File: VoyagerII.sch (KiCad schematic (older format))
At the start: 29 parts, among them P1 TC2030-IDC, SW1 SW_PUSH, U1 ATXMEGA32A4U-AU, U2 MCP1700T-3002E/TT, U3 PRTR5V0U2X, U4 IS31FL3731-SALS2

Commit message: Temporary progress save
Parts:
- R8, R9: renamed from R?; footprint (none) -> Resistors_SMD:R_0805
- gave numbers to parts that had none: 5
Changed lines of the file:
@@
 $EndComp
 $Comp
-L GND #PWR06
+L GND #PWR05
 U 1 1 5A624D2D
 P 4300 1500
-F 0 "#PWR06" H 4300 1250 50  0001 C CNN
+F 0 "#PWR05" H 4300 1250 50  0001 C CNN
 F 1 "GND" H 4300 1350 50  0000 C CNN
 F 2 "" H 4300 1500 50  0001 C CNN
@@
 $EndComp
 $Comp
-L +3.3V #PWR07
+L +3.3V #PWR06
 U 1 1 5A625634
 P 2550 2300
-F 0 "#PWR07" H 2550 2150 50  0001 C CNN
+F 0 "#PWR06" H 2550 2150 50  0001 C CNN
 F 1 "+3.3V" H 2550 2440 50  0000 C CNN
 F 2 "" H 2550 2300 50  0000 C CNN
@@
 $EndComp
 $Comp
-L GND #PWR08
+L GND #PWR07
 U 1 1 5A625723
 P 1900 2500
-F 0 "#PWR08" H 1900 2250 50  0001 C CNN
+F 0 "#PWR07" H 1900 2250 50  0001 C CNN
 F 1 "GND" H 1900 2350 50  0000 C CNN
 F 2 "" H 1900 2500 50  0000 C CNN
@@
 PDI_CLK
 $Comp
-L GND #PWR09
+L GND #PWR08
 U 1 1 5A62606A
 P 1650 2625
-F 0 "#PWR09" H 1650 2375 50  0001 C CNN
+F 0 "#PWR08" H 1650 2375 50  0001 C CNN
 F 1 "GND" H 1650 2475 50  0000 C CNN
 F 2 "" H 1650 2625 50  0000 C CNN
@@
 PDI
 $Comp
-L +3.3V #PWR010
+L +3.3V #PWR09
 U 1 1 5A6265F5
 P 3575 2050
-F 0 "#PWR010" H 3575 1900 50  0001 C CNN
+F 0 "#PWR09" H 3575 1900 50  0001 C CNN
 F 1 "+3.3V" H 3575 2190 50  0000 C CNN
 F 2 "" H 3575 2050 50  0000 C CNN
@@
 $EndComp
 $Comp
-L GND #PWR011
+L GND #PWR010
 U 1 1 5A626934
 P 3825 4950
-F 0 "#PWR011" H 3825 4700 50  0001 C CNN
+F 0 "#PWR010" H 3825 4700 50  0001 C CNN
 F 1 "GND" H 3825 4800 50  0000 C CNN
 F 2 "" H 3825 4950 50  0000 C CNN
@@
 $EndComp
 $Comp
-L +3.3V #PWR012
+L +3.3V #PWR011
 U 1 1 5A627061
 P 725 3075
-F 0 "#PWR012" H 725 2925 50  0001 C CNN
+F 0 "#PWR011" H 725 2925 50  0001 C CNN
 F 1 "+3.3V" H 725 3215 50  0000 C CNN
 F 2 "" H 725 3075 50  0000 C CNN
@@
 $EndComp
 $Comp
-L GND #PWR013
+L GND #PWR012
 U 1 1 5A62709B
 P 725 3275
-F 0 "#PWR013" H 725 3025 50  0001 C CNN
+F 0 "#PWR012" H 725 3025 50  0001 C CNN
 F 1 "GND" H 725 3125 50  0000 C CNN
 F 2 "" H 725 3275 50  0000 C CNN
@@
 $EndComp
 $Comp
-L +3.3V #PWR014
+L +3.3V #PWR013
 U 1 1 5A62AFDE
 P 1650 2425
-F 0 "#PWR014" H 1650 2275 50  0001 C CNN
+F 0 "#PWR013" H 1650 2275 50  0001 C CNN
 F 1 "+3.3V" H 1650 2565 50  0000 C CNN
 F 2 "" H 1650 2425 50  0001 C CNN
@@
 $EndComp
 $Comp
-L GND #PWR015
+L GND #PWR014
 U 1 1 5A64D83E
 P 5600 3550
-F 0 "#PWR015" H 5600 3300 50  0001 C CNN
+F 0 "#PWR014" H 5600 3300 50  0001 C CNN
 F 1 "GND" H 5600 3400 50  0000 C CNN
 F 2 "" H 5600 3550 50  0001 C CNN
@@
 I2C-
 $Comp
-L +5V #PWR016
+L +5V #PWR015
 U 1 1 5A64EBF7
 P 6075 3050
-F 0 "#PWR016" H 6075 2900 50  0001 C CNN
+F 0 "#PWR015" H 6075 2900 50  0001 C CNN
 F 1 "+5V" H 6075 3190 50  0000 C CNN
 F 2 "" H 6075 3050 50  0001 C CNN
@@
 $EndComp
 $Comp
-L GND #PWR017
+L GND #PWR016
 U 1 1 5A64FC3C
 P 7900 4175
-F 0 "#PWR017" H 7900 3925 50  0001 C CNN
+F 0 "#PWR016" H 7900 3925 50  0001 C CNN
 F 1 "GND" H 7900 4025 50  0000 C CNN
 F 2 "" H 7900 4175 50  0001 C CNN
@@
 $EndSheet
 $Comp
-L +3.3V #PWR018
+L +3.3V #PWR017
 U 1 1 5A6EE2A3
 P 8300 3450
-F 0 "#PWR018" H 8300 3300 50  0001 C CNN
+F 0 "#PWR017" H 8300 3300 50  0001 C CNN
 F 1 "+3.3V" H 8300 3590 50  0000 C CNN
 F 2 "" H 8300 3450 50  0001 C CNN
@@
 $EndComp
 $Comp
-L GND #PWR019
+L GND #PWR018
 U 1 1 5A6F9F51
 P 9250 1825
-F 0 "#PWR019" H 9250 1575 50  0001 C CNN
+F 0 "#PWR018" H 9250 1575 50  0001 C CNN
 F 1 "GND" H 9250 1675 50  0000 C CNN
 F 2 "" H 9250 1825 50  0001 C CNN
@@
 NoConn ~ 8325 1175
 $Comp
-L D_Schottky D?
+L D_Schottky D45
 U 1 1 5A83BE64
 P 5150 1300
-F 0 "D?" H 5150 1400 50  0000 C CNN
+F 0 "D45" H 5150 1400 50  0000 C CNN
 F 1 "D_Schottky" H 5150 1200 50  0000 C CNN
 F 2 "" H 5150 1300 50  0001 C CNN
@@
 $EndComp
 $Comp
-L D_Schottky D?
+L D_Schottky D65
 U 1 1 5A83BED8
 P 5550 1300
-F 0 "D?" H 5550 1400 50  0000 C CNN
+F 0 "D65" H 5550 1400 50  0000 C CNN
 F 1 "D_Schottky" H 5550 1200 50  0000 C CNN
 F 2 "" H 5550 1300 50  0001 C CNN
@@
 $EndComp
 $Comp
-L Battery BT?
+L Battery BT1
 U 1 1 5A83C08A
 P 6025 1500
-F 0 "BT?" H 6125 1600 50  0000 L CNN
+F 0 "BT1" H 6125 1600 50  0000 L CNN
 F 1 "Battery" H 6125 1500 50  0000 L CNN
 F 2 "" V 6025 1560 50  0001 C CNN
@@
 	6025 1300 5700 1300
 $Comp
-L GND #PWR?
+L GND #PWR019
 U 1 1 5A83C2DF
 P 6025 1700
-F 0 "#PWR?" H 6025 1450 50  0001 C CNN
+F 0 "#PWR019" H 6025 1450 50  0001 C CNN
 F 1 "GND" H 6025 1550 50  0000 C CNN
 F 2 "" H 6025 1700 50  0001 C CNN
@@
 Connection ~ 5350 1300
 $Comp
-L +3.3V #PWR?
+L +3.3V #PWR020
 U 1 1 5A83C4F3
 P 5350 1075
-F 0 "#PWR?" H 5350 925 50  0001 C CNN
+F 0 "#PWR020" H 5350 925 50  0001 C CNN
 F 1 "+3.3V" H 5350 1215 50  0000 C CNN
 F 2 "" H 5350 1075 50  0001 C CNN
@@
 $EndComp
 $Comp
-L Jumper_NC_Small JP?
+L Jumper_NC_Small JP1
 U 1 1 5A83C91E
 P 5150 1575
-F 0 "JP?" H 5150 1655 50  0000 C CNN
+F 0 "JP1" H 5150 1655 50  0000 C CNN
 F 1 "WirelessJumper" H 5160 1515 50  0000 C CNN
 F 2 "" H 5150 1575 50  0001 C CNN
@@
 	5000 1575 5050 1575
 $Comp
-L R_Small R?
+L R_Small R8
 U 1 1 5A83D067
 P 2125 3425
-F 0 "R?" H 2155 3445 50  0000 L CNN
+F 0 "R8" H 2155 3445 50  0000 L CNN
 F 1 "100k" H 2155 3385 50  0000 L CNN
-F 2 "" H 2125 3425 50  0001 C CNN
+F 2 "Resistors_SMD:R_0805" H 2125 3425 50  0001 C CNN
 F 3 "" H 2125 3425 50  0001 C CNN
 	1    2125 3425
@@
 $EndComp
 $Comp
-L R_Small R?
+L R_Small R9
 U 1 1 5A83D1E3
 P 2125 3675
-F 0 "R?" H 2155 3695 50  0000 L CNN
+F 0 "R9" H 2155 3695 50  0000 L CNN
 F 1 "100k" H 2155 3635 50  0000 L CNN
-F 2 "" H 2125 3675 50  0001 C CNN
+F 2 "Resistors_SMD:R_0805" H 2125 3675 50  0001 C CNN
 F 3 "" H 2125 3675 50  0001 C CNN
 	1    2125 3675
@@
 Connection ~ 2125 3550
 $Comp
-L GND #PWR?
+L GND #PWR021
 U 1 1 5A83D3AD
 P 2125 3800
-F 0 "#PWR?" H 2125 3550 50  0001 C CNN
+F 0 "#PWR021" H 2125 3550 50  0001 C CNN
 F 1 "GND" H 2125 3650 50  0000 C CNN
 F 2 "" H 2125 3800 50  0001 C CNN
@@
 	2125 3800 2125 3775
 $Comp
-L +5V #PWR?
+L +5V #PWR022
 U 1 1 5A83D67E
 P 2125 3300
-F 0 "#PWR?" H 2125 3150 50  0001 C CNN
+F 0 "#PWR022" H 2125 3150 50  0001 C CNN
 F 1 "+5V" H 2125 3440 50  0000 C CNN
 F 2 "" H 2125 3300 50  0001 C CNN
@@
 	2125 3300 2125 3325
 $Comp
-L nRF24L01+ U?
+L nRF24L01+ U6
 U 1 1 5A83C674
 P 5300 5375
-F 0 "U?" H 4950 5625 60  0000 C CNN
+F 0 "U6" H 4950 5625 60  0000 C CNN
 F 1 "nRF24L01+" H 5300 5525 60  0000 C CNN
 F 2 "mysensors_radios:NRF24L01" H 5150 5175 60  0000 C CNN
@@
 $EndComp
 $Comp
-L +3.3V #PWR?
+L +3.3V #PWR023
 U 1 1 5A83C8CF
 P 5650 4975
-F 0 "#PWR?" H 5650 4825 50  0001 C CNN
+F 0 "#PWR023" H 5650 4825 50  0001 C CNN
 F 1 "+3.3V" H 5650 5115 50  0000 C CNN
 F 2 "" H 5650 4975 50  0001 C CNN
@@
 $EndComp
 $Comp
-L GND #PWR?
+L GND #PWR024
 U 1 1 5A83C91D
 P 5550 4975
-F 0 "#PWR?" H 5550 4725 50  0001 C CNN
+F 0 "#PWR024" H 5550 4725 50  0001 C CNN
 F 1 "GND" H 5550 4825 50  0000 C CNN
 F 2 "" H 5550 4975 50  0001 C CNN

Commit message: Revert wireless functionality
Not this time.
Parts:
- removed BT1: Battery, symbol Battery
- removed D45, D65: D_Schottky, symbol D_Schottky
- removed JP1: WirelessJumper, symbol Jumper_NC_Small
- removed R8, R9: 100k, Resistors_SMD:R_0805, symbol R_Small
- removed U6: nRF24L01+, mysensors_radios:NRF24L01, symbol nRF24L01+
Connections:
- wire segments 92 -> 74
- no-connect marks 4 -> 2
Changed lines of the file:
@@
 	1    0    0    -1
 $EndComp
-Wire Wire Line
-	4225 1300 5000 1300
 Connection ~ 4300 1300
 Wire Wire Line
@@
 NoConn ~ 8325 1175
 $Comp
-L D_Schottky D45
-U 1 1 5A83BE64
-P 5150 1300
-F 0 "D45" H 5150 1400 50  0000 C CNN
-F 1 "D_Schottky" H 5150 1200 50  0000 C CNN
-F 2 "" H 5150 1300 50  0001 C CNN
-F 3 "" H 5150 1300 50  0001 C CNN
-	1    5150 1300
-	-1   0    0    1
-$EndComp
-$Comp
-L D_Schottky D65
-U 1 1 5A83BED8
-P 5550 1300
-F 0 "D65" H 5550 1400 50  0000 C CNN
-F 1 "D_Schottky" H 5550 1200 50  0000 C CNN
-F 2 "" H 5550 1300 50  0001 C CNN
-F 3 "" H 5550 1300 50  0001 C CNN
-	1    5550 1300
-	1    0    0    -1
-$EndComp
-$Comp
-L Battery BT1
-U 1 1 5A83C08A
-P 6025 1500
-F 0 "BT1" H 6125 1600 50  0000 L CNN
-F 1 "Battery" H 6125 1500 50  0000 L CNN
-F 2 "" V 6025 1560 50  0001 C CNN
-F 3 "" V 6025 1560 50  0001 C CNN
-	1    6025 1500
-	1    0    0    -1
-$EndComp
-Wire Wire Line
-	6025 1300 5700 1300
-$Comp
-L GND #PWR019
-U 1 1 5A83C2DF
-P 6025 1700
-F 0 "#PWR019" H 6025 1450 50  0001 C CNN
-F 1 "GND" H 6025 1550 50  0000 C CNN
-F 2 "" H 6025 1700 50  0001 C CNN
-F 3 "" H 6025 1700 50  0001 C CNN
-	1    6025 1700
-	1    0    0    -1
-$EndComp
-Wire Wire Line
-	5300 1300 5400 1300
-Wire Wire Line
-	5350 1075 5350 1575
-Connection ~ 5350 1300
-$Comp
 L +3.3V #PWR020
 U 1 1 5A83C4F3
-P 5350 1075
-F 0 "#PWR020" H 5350 925 50  0001 C CNN
-F 1 "+3.3V" H 5350 1215 50  0000 C CNN
-F 2 "" H 5350 1075 50  0001 C CNN
-F 3 "" H 5350 1075 50  0001 C CNN
-	1    5350 1075
-	1    0    0    -1
-$EndComp
-$Comp
-L Jumper_NC_Small JP1
-U 1 1 5A83C91E
-P 5150 1575
-F 0 "JP1" H 5150 1655 50  0000 C CNN
-F 1 "WirelessJumper" H 5160 1515 50  0000 C CNN
-F 2 "" H 5150 1575 50  0001 C CNN
-F 3 "" H 5150 1575 50  0001 C CNN
-	1    5150 1575
-	1    0    0    -1
-$EndComp
-Wire Wire Line
-	5350 1575 5250 1575
-Wire Wire Line
-	5000 1300 5000 1575
-Wire Wire Line
-	5000 1575 5050 1575
-$Comp
-L R_Small R8
-U 1 1 5A83D067
-P 2125 3425
-F 0 "R8" H 2155 3445 50  0000 L CNN
-F 1 "100k" H 2155 3385 50  0000 L CNN
-F 2 "Resistors_SMD:R_0805" H 2125 3425 50  0001 C CNN
-F 3 "" H 2125 3425 50  0001 C CNN
-	1    2125 3425
-	1    0    0    -1
-$EndComp
-$Comp
-L R_Small R9
-U 1 1 5A83D1E3
-P 2125 3675
-F 0 "R9" H 2155 3695 50  0000 L CNN
-F 1 "100k" H 2155 3635 50  0000 L CNN
-F 2 "Resistors_SMD:R_0805" H 2125 3675 50  0001 C CNN
-F 3 "" H 2125 3675 50  0001 C CNN
-	1    2125 3675
-	1    0    0    -1
-$EndComp
-Wire Wire Line
-	2125 3525 2125 3575
-Wire Wire Line
-	2125 3550 2775 3550
-Connection ~ 2125 3550
-$Comp
-L GND #PWR021
-U 1 1 5A83D3AD
-P 2125 3800
-F 0 "#PWR021" H 2125 3550 50  0001 C CNN
-F 1 "GND" H 2125 3650 50  0000 C CNN
-F 2 "" H 2125 3800 50  0001 C CNN
-F 3 "" H 2125 3800 50  0001 C CNN
-	1    2125 3800
-	1    0    0    -1
-$EndComp
-Wire Wire Line
-	2125 3800 2125 3775
-$Comp
-L +5V #PWR022
-U 1 1 5A83D67E
-P 2125 3300
-F 0 "#PWR022" H 2125 3150 50  0001 C CNN
-F 1 "+5V" H 2125 3440 50  0000 C CNN
-F 2 "" H 2125 3300 50  0001 C CNN
-F 3 "" H 2125 3300 50  0001 C CNN
-	1    2125 3300
-	1    0    0    -1
-$EndComp
-Wire Wire Line
-	2125 3300 2125 3325
-$Comp
-L nRF24L01+ U6
-U 1 1 5A83C674
-P 5300 5375
-F 0 "U6" H 4950 5625 60  0000 C CNN
-F 1 "nRF24L01+" H 5300 5525 60  0000 C CNN
-F 2 "mysensors_radios:NRF24L01" H 5150 5175 60  0000 C CNN
-F 3 "" H 5150 5175 60  0000 C CNN
-	1    5300 5375
-	-1   0    0    1
-$EndComp
-$Comp
-L +3.3V #PWR023
-U 1 1 5A83C8CF
-P 5650 4975
-F 0 "#PWR023" H 5650 4825 50  0001 C CNN
-F 1 "+3.3V" H 5650 5115 50  0000 C CNN
-F 2 "" H 5650 4975 50  0001 C CNN
-F 3 "" H 5650 4975 50  0001 C CNN
-	1    5650 4975
-	1    0    0    -1
-$EndComp
-$Comp
-L GND #PWR024
-U 1 1 5A83C91D
-P 5550 4975
-F 0 "#PWR024" H 5550 4725 50  0001 C CNN
-F 1 "GND" H 5550 4825 50  0000 C CNN
-F 2 "" H 5550 4975 50  0001 C CNN
-F 3 "" H 5550 4975 50  0001 C CNN
-	1    5550 4975
-	-1   0    0    1
-$EndComp
-NoConn ~ 5450 4975
-Wire Wire Line
-	4575 4200 5350 4200
-Wire Wire Line
-	5350 4200 5350 4975
-Wire Wire Line
-	4575 4300 5150 4300
-Wire Wire Line
-	5150 4300 5150 4975
-Wire Wire Line
-	4575 4400 5050 4400
-Wire Wire Line
-	5050 4400 5050 4975
-NoConn ~ 4950 4975
-Wire Wire Line
-	4575 4500 5250 4500
-Wire Wire Line
-	5250 4500 5250 4975
+P 4550 1300
+F 0 "#PWR020" H 4550 1150 50  0001 C CNN
+F 1 "+3.3V" H 4550 1440 50  0000 C CNN
+F 2 "" H 4550 1300 50  0001 C CNN
+F 3 "" H 4550 1300 50  0001 C CNN
+	1    4550 1300
+	0    1    1    0
+$EndComp
+Wire Wire Line
+	4225 1300 4550 1300
 $EndSCHEMATC

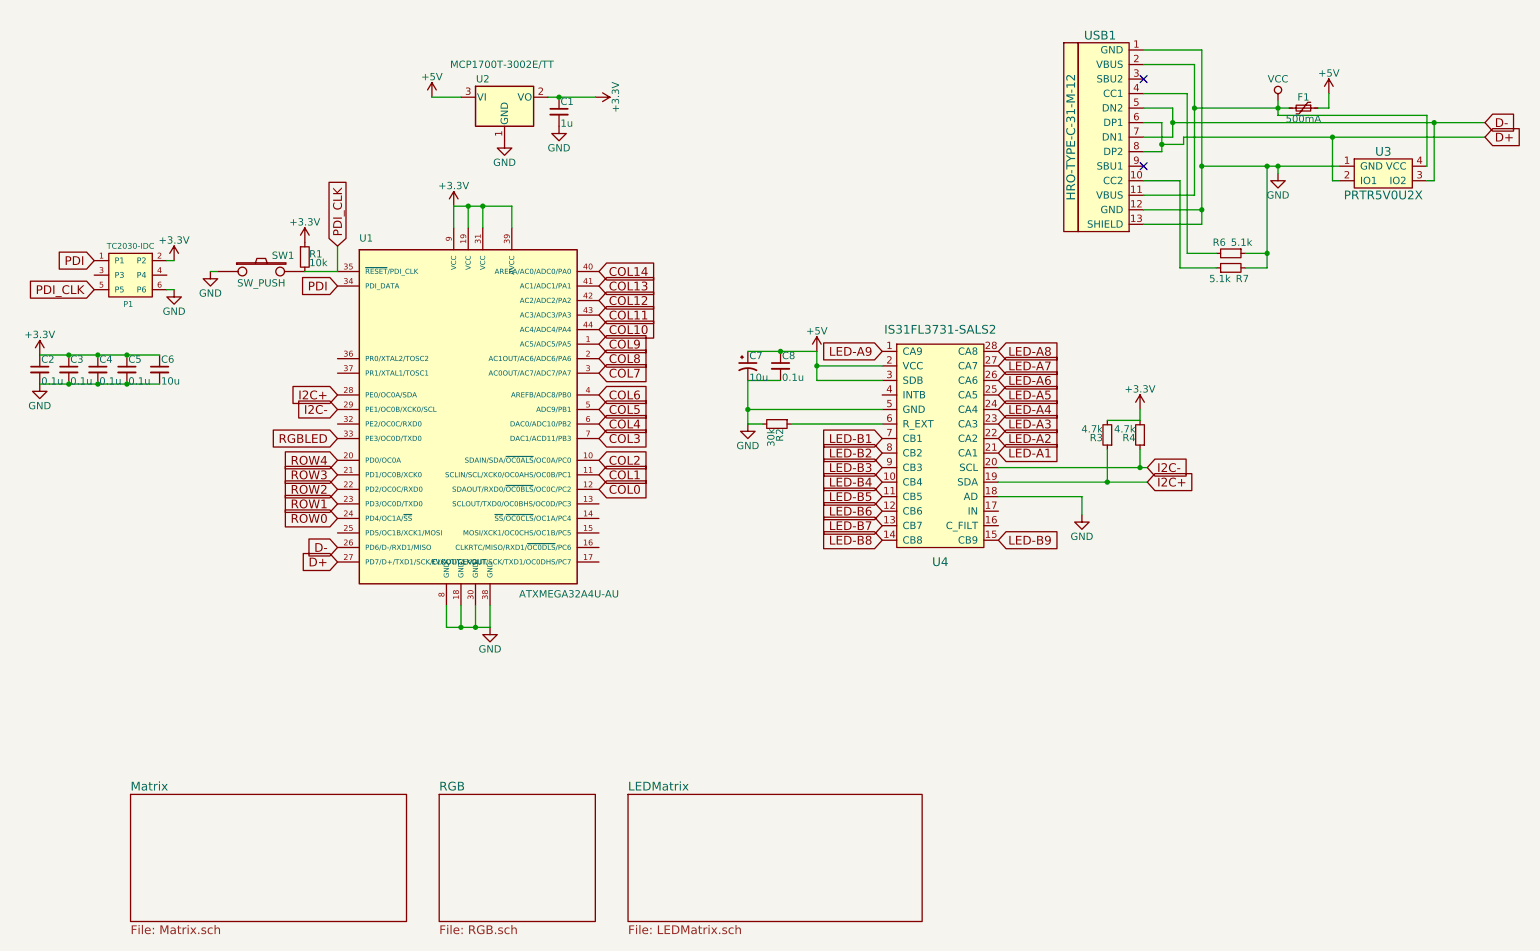
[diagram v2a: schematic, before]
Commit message: Swap LED controller for IS31FL3733
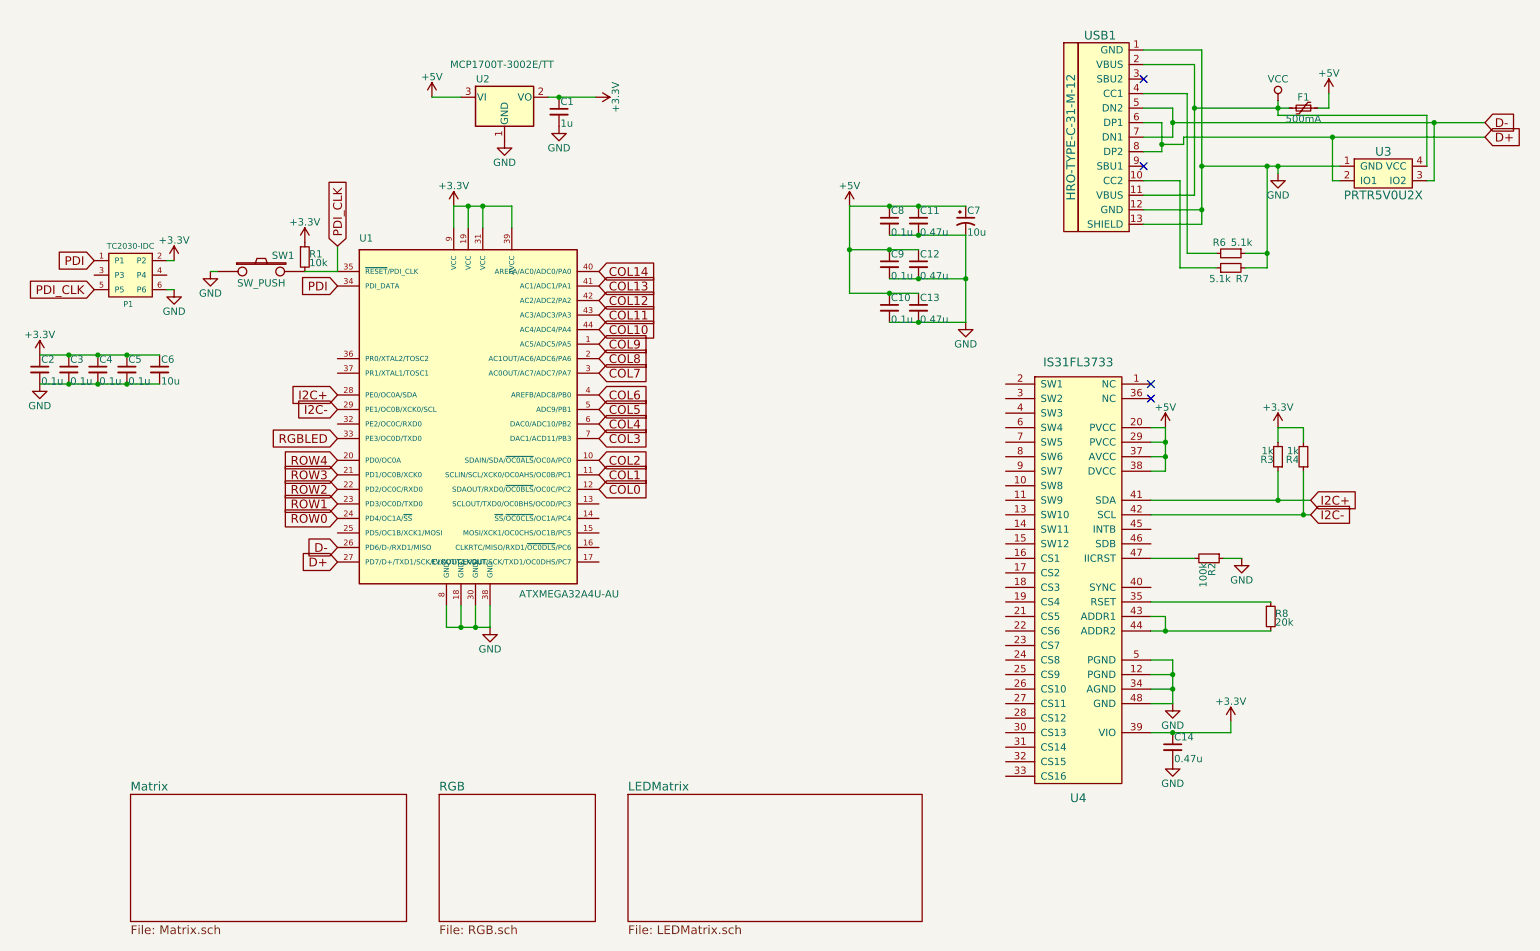
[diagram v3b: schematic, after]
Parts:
- removed U4: IS31FL3731-SALS2, Housings_SSOP:SSOP-28_5.3x10.2mm_Pitch0.65mm, symbol IS31FL3731-SALS2
- added C10, C9: 0.1u, Capacitors_SMD:C_0805, symbol C_Small
- added C11, C12, C13, C14: 0.47u, Capacitors_SMD:C_0805, symbol C_Small
- added R8: 20k, Resistors_SMD:R_0805, symbol R_Small
- added U4: IS31FL3733, symbol IS31FL3733
- R2: value 30k -> 100k
- R3, R4: value 4.7k -> 1k
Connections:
- net +3V3: now also C14.1, U4.39 (VIO)
- net +5V: now also C10.1, C11.1, C12.1, C13.1, C9.1, U4.20 (PVCC), U4.29 (PVCC), U4.37 (AVCC), U4.38 (DVCC)
- net GND: now also R2.1, C10.2, C11.2, C12.2, C13.2, C14.2, C9.2, U4.12 (PGND), U4.34 (AGND), U4.48 (GND), U4.5 (PGND); no longer R2.2
- net I2C+: now also U4.41 (SDA)
- net I2C-: now also U4.42 (SCL)
- new net: R8.1, U4.35 (RSET)
- new net: R8.2, U4.43 (ADDR1), U4.44 (ADDR2)
- new net: R2.2, U4.47 (IICRST)
- no-connect marks 2 -> 4
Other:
- moved on the sheet: C7, C8, R3, R4
